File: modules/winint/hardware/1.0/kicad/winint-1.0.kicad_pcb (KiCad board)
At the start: 2 copper layers, 75 x 75 mm, 61 parts, among them J1 Screw_Terminal_01x09, J2 Screw_Terminal_01x09, J3 M12-5PIN, J4 RELAYS, K1 SANYOU_SRD_Form_C, K2 SANYOU_SRD_Form_C, Q1 2N2219, Q2 2N2219, SW1 INSTANCE, U1 ROT, U2 DOK, U3 STP, U4 DEP, U5 RET, U6 OVL, U7 Teensy_3.2, U8 TEC2-2411WI, U9 MCP2551-I-P

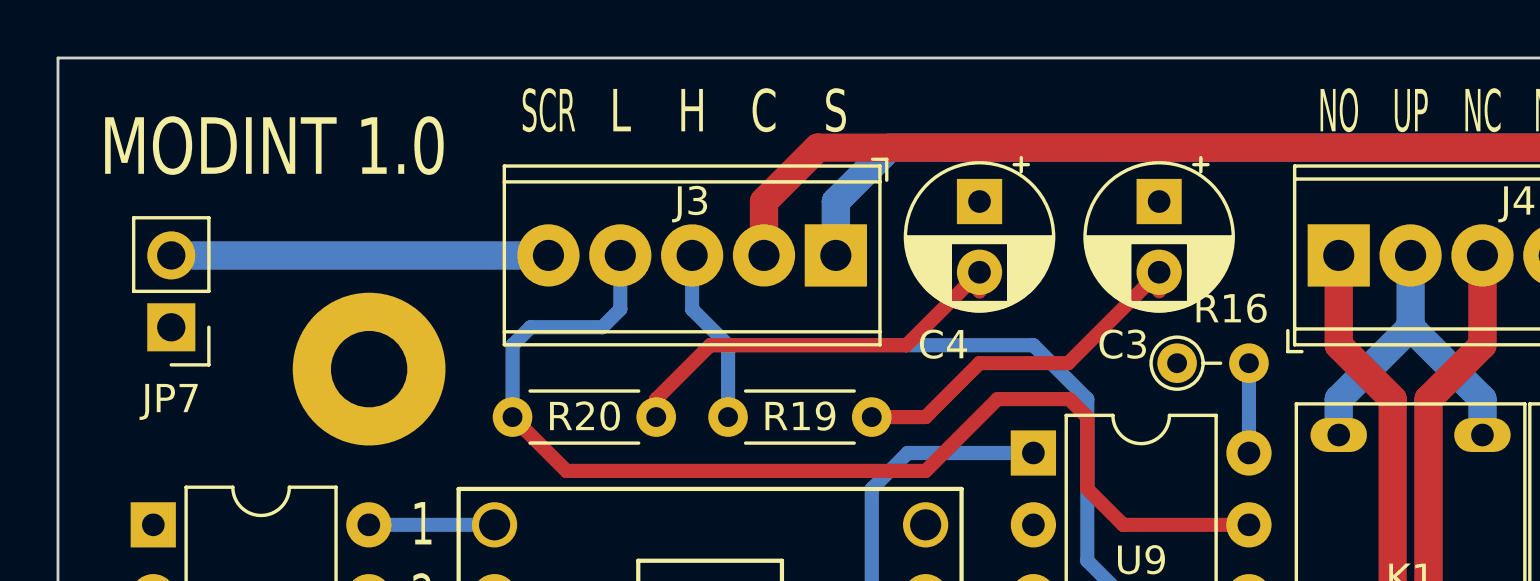
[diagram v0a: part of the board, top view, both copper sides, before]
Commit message: README edit
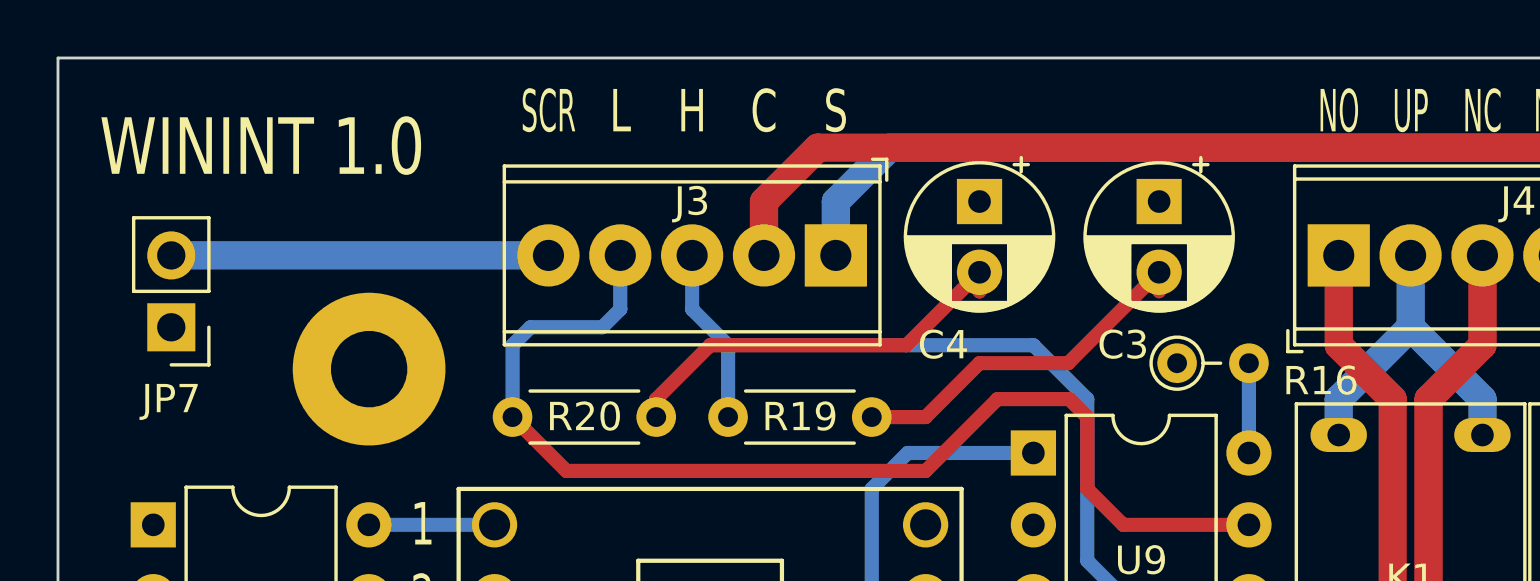
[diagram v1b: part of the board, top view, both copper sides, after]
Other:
- board text added: "WININT 1.0"
- board text removed: "MODINT 1.0"
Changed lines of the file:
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@@
   (layers
     (0 F.Cu signal hide)
-    (31 B.Cu signal hide)
+    (31 B.Cu signal)
     (33 F.Adhes user hide)
     (35 F.Paste user hide)
@@
   )
   (setup
-    (last_trace_width 0.5)
+    (last_trace_width 0.25)
     (user_trace_width 0.5)
     (user_trace_width 1)
@@
     (descr "Resistor, Axial_DIN0204 series, Axial, Vertical, pin pitch=2.54mm, 0.167W, length*diameter=3.6*1.6mm^2, http://cdn-reichelt.de/documents/datenblatt/B400/1_4W%23YAG.pdf")
     (tags "Resistor Axial_DIN0204 series Axial Vertical pin pitch 2.54mm 0.167W length 3.6mm diameter 1.6mm")
-    (fp_text reference R16 (at 1.905 -1.905) (layer F.SilkS)
+    (fp_text reference R16 (at 5.08 0.635) (layer F.SilkS)
       (effects (font (size 1 1) (thickness 0.15)))
     )
@@
     (effects (font (size 1.5 1) (thickness 0.2)))
   )
-  (gr_text "MODINT 1.0\n" (at 137.465 90.17) (layer F.SilkS)
+  (gr_text "WININT 1.0\n" (at 137.465 90.17) (layer F.SilkS)
     (effects (font (size 2 1.5) (thickness 0.3)) (justify left))
   )

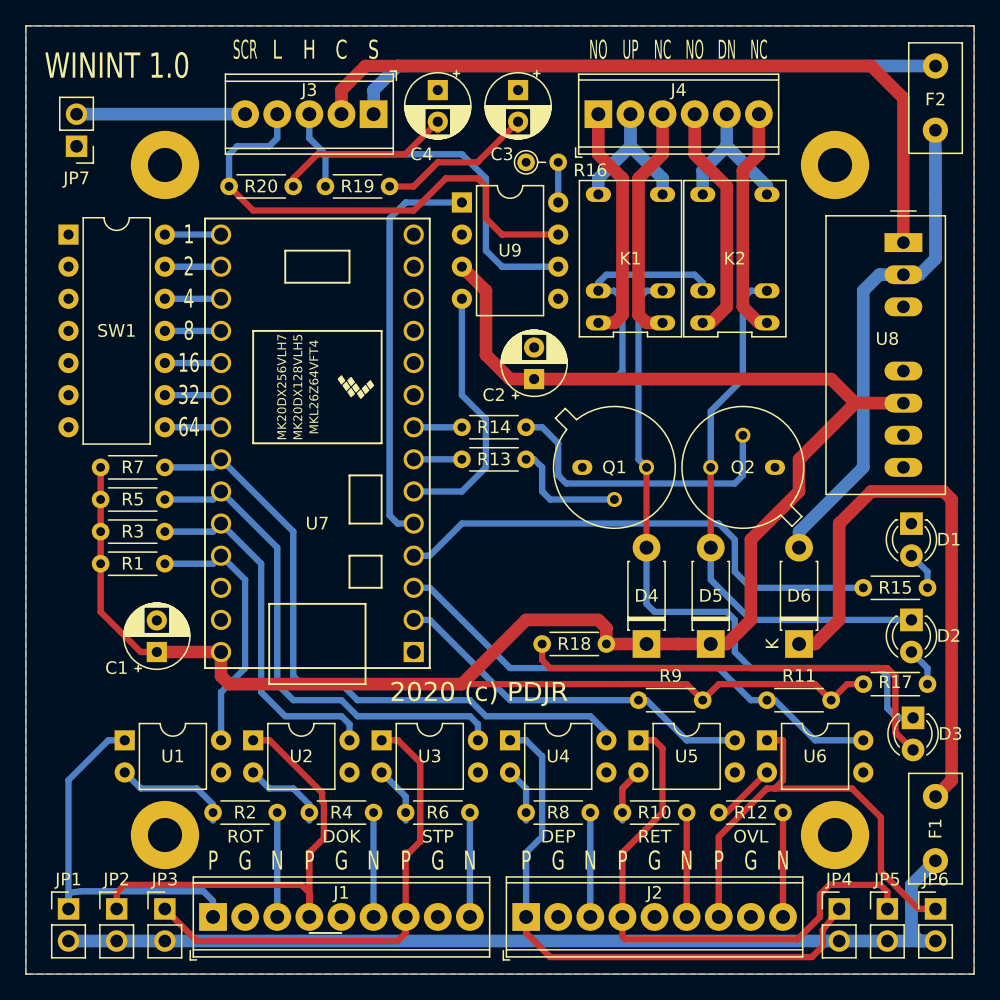
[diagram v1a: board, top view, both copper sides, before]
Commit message: Added snubber circuit to relay NO output
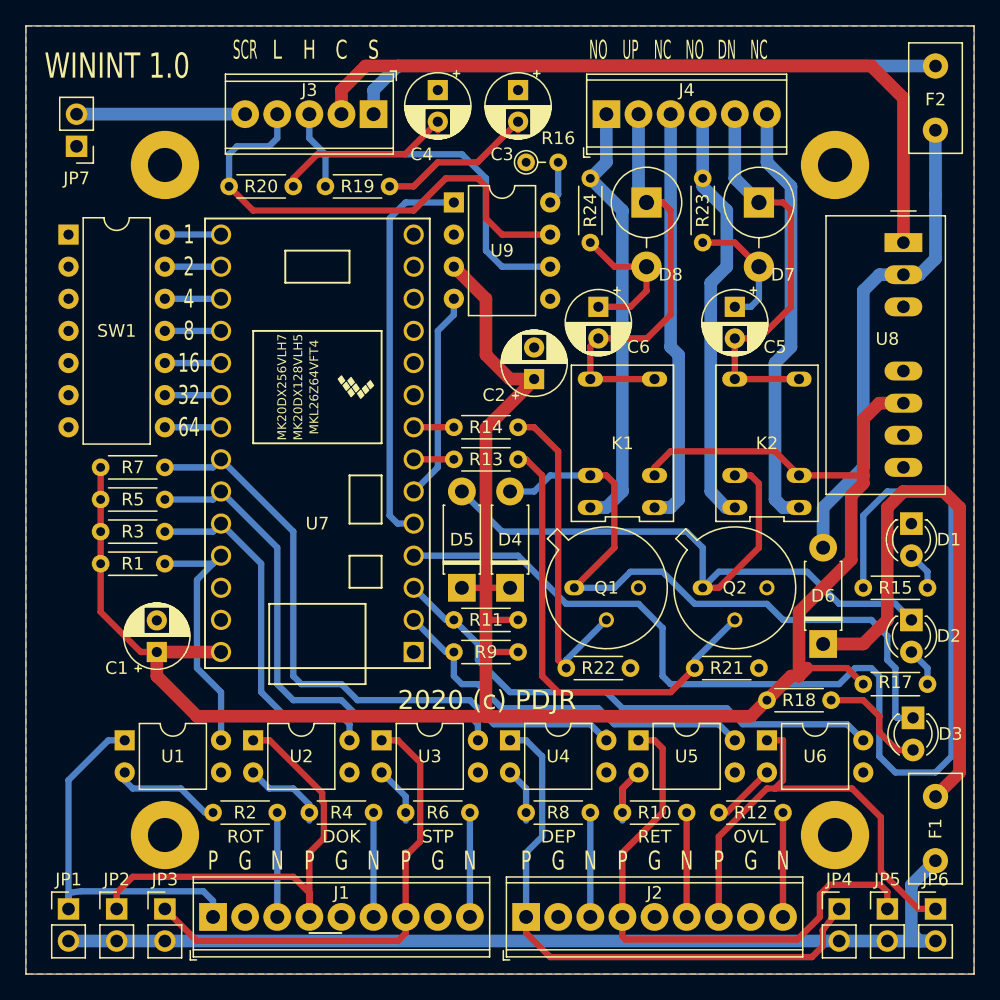
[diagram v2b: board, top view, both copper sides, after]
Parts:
- added C5: 33n, Capacitor_THT:CP_Radial_D5.0mm_P2.50mm, F.Cu at (192.1, 109.2)
- added C6: 33n, Capacitor_THT:CP_Radial_D5.0mm_P2.50mm, F.Cu at (181.3, 109.2)
- added D7: D_TVS, Diode_THT:D_DO-27_P5.08mm_Vertical_AnodeUp, F.Cu at (194.0, 101.0)
- added D8: D_TVS, Diode_THT:D_DO-27_P5.08mm_Vertical_AnodeUp, F.Cu at (185.1, 101.0)
- added R21: 4K7, Resistor_THT:R_Axial_DIN0204_L3.6mm_D1.6mm_P5.08mm_Horizontal, F.Cu at (194.0, 137.8)
- added R22: 4K7, Resistor_THT:R_Axial_DIN0204_L3.6mm_D1.6mm_P5.08mm_Horizontal, F.Cu at (178.7, 137.8)
- added R23: 43R, Resistor_THT:R_Axial_DIN0204_L3.6mm_D1.6mm_P5.08mm_Horizontal, F.Cu at (189.5, 104.1)
- added R24: 43R, Resistor_THT:R_Axial_DIN0204_L3.6mm_D1.6mm_P5.08mm_Horizontal, F.Cu at (180.6, 99.1)
- moved R11 25.6 mm to (169.8, 134.0)
- moved R18 23.3 mm to (199.7, 140.3), turned to 180 degrees
- moved D5 20.2 mm to (170.5, 131.4)
- moved R9 15.1 mm to (169.8, 136.5)
- moved K2 14.8 mm to (194.6, 120.0)
- moved K1 14.6 mm to (183.2, 120.0)
- moved D4 11.7 mm to (174.3, 131.4)
- moved Q2 11.1 mm to (189.5, 131.4), turned to 0 degrees
- moved Q1 9.55 mm to (179.4, 131.4)
- moved D6 1.91 mm to (199.1, 135.9)
- moved U9 0.64 mm to (169.8, 101.0)
- moved J4 0.63 mm to (181.9, 94.0)
- moved R13 0.63 mm to (174.9, 121.3)
- moved R14 0.63 mm to (174.9, 118.7)
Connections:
- K1 pad 2: Net-(D3-Pad1) -> Net-(C1-Pad1)
- K1 pad 9: Net-(C1-Pad1) -> Net-(D3-Pad1)
- K2 pad 2: Net-(D2-Pad1) -> Net-(C1-Pad1)
- K2 pad 9: Net-(C1-Pad1) -> Net-(D2-Pad1)
- Q1 pad 1: GND -> Net-(D3-Pad1)
- Q1 pad 3: Net-(D3-Pad1) -> GND
- Q2 pad 1: GND -> Net-(D2-Pad1)
- Q2 pad 3: Net-(D2-Pad1) -> GND
- R13 pad 1: Net-(Q1-Pad2) -> Net-(Q2-Pad2)
- R14 pad 1: Net-(Q2-Pad2) -> Net-(Q1-Pad2)
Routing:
- net Net-(R15-Pad1): track 40.2 -> 91.2 mm
- net Net-(D3-Pad2): track 36.2 -> 8.85 mm
- net Net-(C6-Pad2): track 12.3 -> 32.7 mm
- net Net-(C5-Pad2): track 12.3 -> 32.0 mm
- net Net-(Q1-Pad2): track 9.42 -> 26.5 mm
- net Net-(J4-Pad6): track 18.2 -> 34.0 mm
- net Net-(J4-Pad1): track 18.8 -> 34.5 mm
- net Net-(C1-Pad1): track 192.7 -> 177.8 mm
- net Net-(J4-Pad4): track 18.7 -> 33.6 mm
- net Net-(J4-Pad3): track 18.8 -> 32.9 mm
- net Net-(D2-Pad1): track 42.6 -> 55.7 mm
- net Net-(Q2-Pad2): track 23.9 -> 36.8 mm
- net Net-(C6-Pad1): track 0.00 -> 11.5 mm
- net Net-(C5-Pad1): track 0.00 -> 9.94 mm
- net Net-(U7-Pad6): track 20.6 -> 16.6 mm
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
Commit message: Revised PCB layout
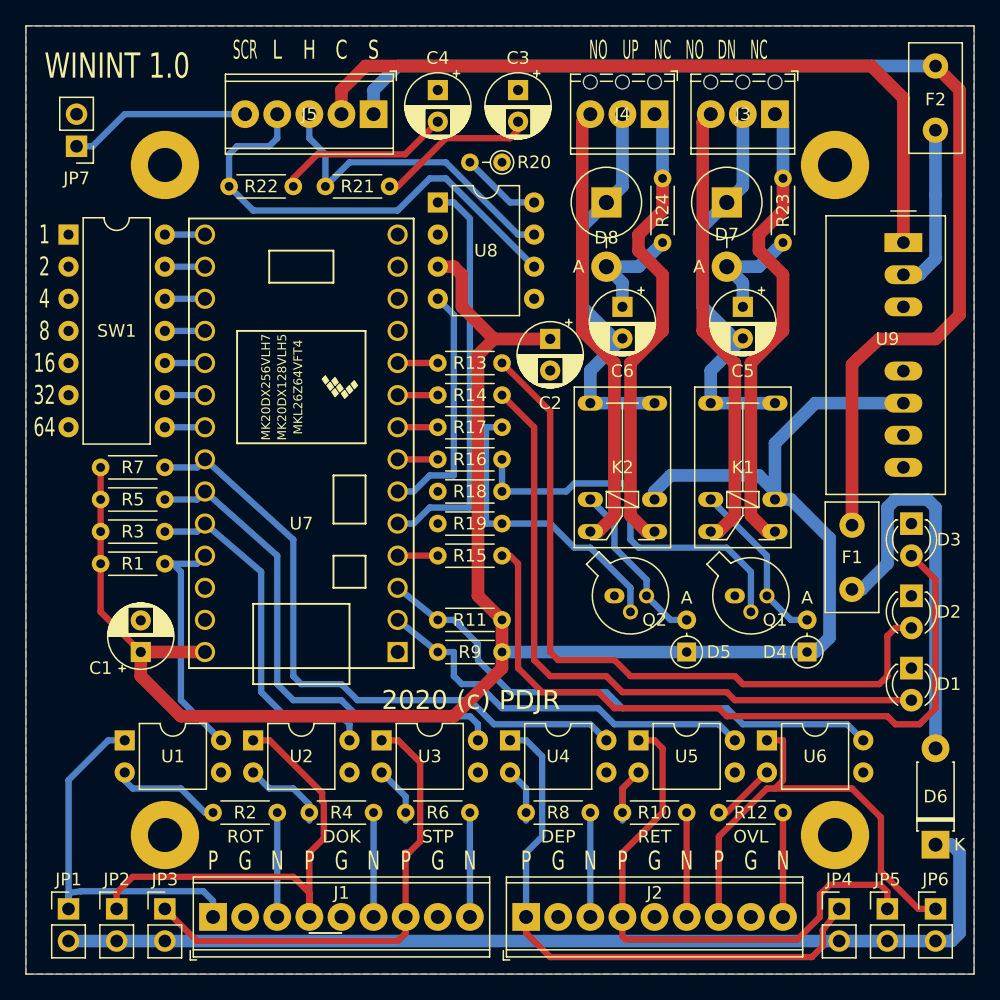
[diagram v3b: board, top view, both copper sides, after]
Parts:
- removed the D3 at (206.2, 141.7)
- removed the D6 at (199.1, 135.9)
- removed the R23 at (189.5, 104.1)
- removed the R24 at (180.6, 99.1)
- removed the U8 at (205.4, 104.1)
- added D1: DOWN, LED_THT:LED_D3.0mm, F.Cu at (206.0, 137.8)
- added D5: 1N4007, Diode_THT:D_DO-34_SOD68_P2.54mm_Vertical_AnodeUp, F.Cu at (188.3, 136.5)
- added J5: Screw_Terminal_01x05, TerminalBlock_Phoenix:TerminalBlock_Phoenix_MPT-0,5-5-2.54_1x05_P2.54mm_Horizontal, F.Cu at (163.5, 94.0)
- added R16: 4K7, Resistor_THT:R_Axial_DIN0204_L3.6mm_D1.6mm_P5.08mm_Horizontal, F.Cu at (173.7, 121.3)
- added R19: 4K7, Resistor_THT:R_Axial_DIN0204_L3.6mm_D1.6mm_P5.08mm_Horizontal, F.Cu at (168.6, 126.4)
- added U9: TEC2-2411WI, Converter_DCDC:Converter_DCDC_TRACO_TMR-xxxx_THT, F.Cu at (205.4, 104.1)
- C2: value 100nF -> 100n
- C3, C4: value 560pF -> 560p
- D2: value DN -> UP
- D4: footprint Diode_THT:D_DO-41_SOD81_P7.62mm_Horizontal -> Diode_THT:D_DO-34_SOD68_P2.54mm_Vertical_AnodeUp
- J3: value M12-5PIN -> Screw_Terminal_01x03; footprint TerminalBlock_Phoenix:TerminalBlock_Phoenix_MPT-0,5-5-2.54_1x05_P2.54mm_Horizontal -> TerminalBlock_Phoenix:TerminalBlock_Phoenix_MPT-0,5-3-2.54_1x03_P2.54mm_Horizontal
- J4: value RELAYS -> Screw_Terminal_01x03; footprint TerminalBlock_Phoenix:TerminalBlock_Phoenix_MPT-0,5-6-2.54_1x06_P2.54mm_Horizontal -> TerminalBlock_Phoenix:TerminalBlock_Phoenix_MPT-0,5-3-2.54_1x03_P2.54mm_Horizontal
- K1, K2: footprint PDJR:RS_RELAY_476-757 -> PDJR:476-257
- Q1, Q2: footprint Package_TO_SOT_THT:TO-39-3 -> Package_TO_SOT_THT:TO-18-3
- R13, R14: value 4K7 -> 200R
- R17, R18: value 200R -> 4K7
- R21, R22: value 4K7 -> 100R
- R23: renamed from R19; value 100R -> 43R
- R24: renamed from R20; value 100R -> 43R
- moved R21 51.3 mm to (159.7, 99.7), turned to 0 degrees
- moved R22 43.8 mm to (157.2, 99.7), turned to 180 degrees
- moved D6 42.6 mm to (207.9, 151.8)
- moved R17 39.3 mm to (173.7, 118.7)
- moved R23 36.5 mm to (195.9, 104.1), turned to 90 degrees
- moved R18 35.2 mm to (168.6, 123.8), turned to 0 degrees
- moved R15 33.8 mm to (168.6, 128.9)
- moved J3 31.8 mm to (195.2, 94.0)
- moved R24 29.5 mm to (186.4, 104.1), turned to 90 degrees
- moved D4 24.0 mm to (197.8, 136.5)
- moved F1 22.5 mm to (201.3, 126.5)
- moved Q1 12.7 mm to (192.1, 132.1)
- moved K2 11.6 mm to (183.2, 121.9)
- moved R13 9.92 mm to (168.6, 113.7), turned to 0 degrees
- moved K1 9.71 mm to (192.7, 121.9)
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- renumbered D1 to D3, D5 to D6, R16 to R20, U9 to U8
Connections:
- C1 pad 1: Net-(C1-Pad1) -> /5VDC
- C2 pad 1: Net-(C1-Pad1) -> /5VDC
- D2 pad 1: Net-(D2-Pad1) -> GND
- D4 pad 1: Net-(C1-Pad1) -> /5VDC
- D4 pad 2: Net-(D3-Pad1) -> Net-(D4-Pad2)
- D6 pad 1: Net-(C1-Pad1) -> /12VDC
- D6 pad 2: Net-(D2-Pad1) -> Net-(D6-Pad2)
- F1 pad 1: Net-(D6-Pad1) -> /NETS
- F1 pad 2: Net-(F1-Pad2) -> Net-(D6-Pad2)
- F2 pad 1: Net-(F2-Pad1) -> /NETS
- J3 pad 1: Net-(F2-Pad1) -> Net-(J3-Pad1)
- J3 pad 2: Net-(J3-Pad2) -> Net-(C5-Pad2)
- JP1 pad 2: Net-(F1-Pad2) -> /12VDC
- JP2 pad 2: Net-(F1-Pad2) -> /12VDC
- JP3 pad 2: Net-(F1-Pad2) -> /12VDC
- JP4 pad 2: Net-(F1-Pad2) -> /12VDC
- JP5 pad 2: Net-(F1-Pad2) -> /12VDC
- JP6 pad 2: Net-(F1-Pad2) -> /12VDC
- JP7 pad 1: GND -> /SHIELD
- JP7 pad 2: Net-(J3-Pad5) -> GND
- K1 pad 1: Net-(J4-Pad3) -> Net-(J3-Pad1)
- K1 pad 10: Net-(J4-Pad1) -> Net-(J3-Pad3)
- K1 pad 2: Net-(C1-Pad1) -> /5VDC
- K1 pad 5: Net-(C6-Pad2) -> Net-(C5-Pad2)
- K1 pad 6: Net-(C6-Pad2) -> Net-(C5-Pad2)
- K1 pad 9: Net-(D3-Pad1) -> Net-(D4-Pad2)
- K2 pad 1: Net-(J4-Pad6) -> Net-(J4-Pad1)
- K2 pad 10: Net-(J4-Pad4) -> Net-(J4-Pad3)
- K2 pad 2: Net-(C1-Pad1) -> /5VDC
- K2 pad 5: Net-(C5-Pad2) -> Net-(C6-Pad2)
- K2 pad 6: Net-(C5-Pad2) -> Net-(C6-Pad2)
- K2 pad 9: Net-(D2-Pad1) -> Net-(D5-Pad2)
- Q1 pad 1: Net-(D3-Pad1) -> GND
- Q1 pad 3: GND -> Net-(D4-Pad2)
- Q2 pad 1: Net-(D2-Pad1) -> GND
- Q2 pad 3: GND -> Net-(D5-Pad2)
- R1 pad 2: Net-(C1-Pad1) -> /5VDC
- R11 pad 2: Net-(C1-Pad1) -> /5VDC
- R13 pad 1: Net-(Q2-Pad2) -> Net-(R13-Pad1)
- R13 pad 2: Net-(R13-Pad2) -> Net-(D2-Pad2)
- R14 pad 1: Net-(Q1-Pad2) -> Net-(R14-Pad1)
- R14 pad 2: Net-(R14-Pad2) -> Net-(D1-Pad2)
- R17 pad 1: Net-(D2-Pad2) -> Net-(Q2-Pad2)
- R17 pad 2: Net-(C1-Pad1) -> Net-(R17-Pad2)
- R18 pad 1: Net-(D3-Pad2) (its old number) -> GND
- R18 pad 2: Net-(C1-Pad1) -> Net-(Q1-Pad2)
- R21 pad 1: GND -> /CANH
- R21 pad 2: Net-(Q2-Pad2) -> Net-(C3-Pad2)
- R22 pad 1: Net-(Q1-Pad2) -> Net-(C4-Pad2)
- R22 pad 2: GND -> /CANL
- R23 pad 1: Net-(J3-Pad3) -> Net-(C5-Pad1)
- R23 pad 2: Net-(C3-Pad2) -> Net-(J3-Pad1)
- R24 pad 1: Net-(C4-Pad2) -> Net-(C6-Pad1)
- R24 pad 2: Net-(J3-Pad4) -> Net-(J4-Pad1)
- R3 pad 2: Net-(C1-Pad1) -> /5VDC
- R5 pad 2: Net-(C1-Pad1) -> /5VDC
- R7 pad 2: Net-(C1-Pad1) -> /5VDC
- R9 pad 2: Net-(C1-Pad1) -> /5VDC
- U7 pad 10: (no net) -> Net-(R13-Pad1)
- U7 pad 28: Net-(C1-Pad1) -> /5VDC
- U7 pad 7: Net-(R13-Pad2) -> Net-(R16-Pad2)
- U7 pad 8: Net-(R14-Pad2) -> Net-(R17-Pad2)
- U7 pad 9: (no net) -> Net-(R14-Pad1)
- U8 pad 3: Net-(C1-Pad1) -> /5VDC
- U8 pad 6: Net-(J3-Pad3) -> /CANL
- U8 pad 7: Net-(J3-Pad4) -> /CANH
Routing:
- net /5VDC: track 0.00 -> 183.7 mm
- net Net-(C1-Pad1): track 177.8 -> 0.00 mm
- net /NETS: track 0.00 -> 90.4 mm
- net Net-(R15-Pad1): track 91.2 -> 3.18 mm
- net /12VDC: track 0.00 -> 79.3 mm
- net Net-(F1-Pad2): track 77.3 -> 0.00 mm
- net Net-(J3-Pad2): track 59.6 -> 0.00 mm
- net /NETC: track 0.00 -> 59.6 mm
- net Net-(D2-Pad1): track 55.7 -> 0.00 mm
- net Net-(D3-Pad2): track 3.07 -> 58.0 mm
- net Net-(D2-Pad2): track 3.07 -> 57.8 mm
- net Net-(D3-Pad1): track 54.1 -> 0.00 mm
- net Net-(D1-Pad2): track 0.00 -> 53.2 mm
- net Net-(F2-Pad1): track 47.1 -> 0.00 mm
- net Net-(D6-Pad1): track 45.2 -> 0.00 mm
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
